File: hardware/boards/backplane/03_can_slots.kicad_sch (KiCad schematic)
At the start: 11 parts, among them J8 DC IN, U4 INA237AIDGSR

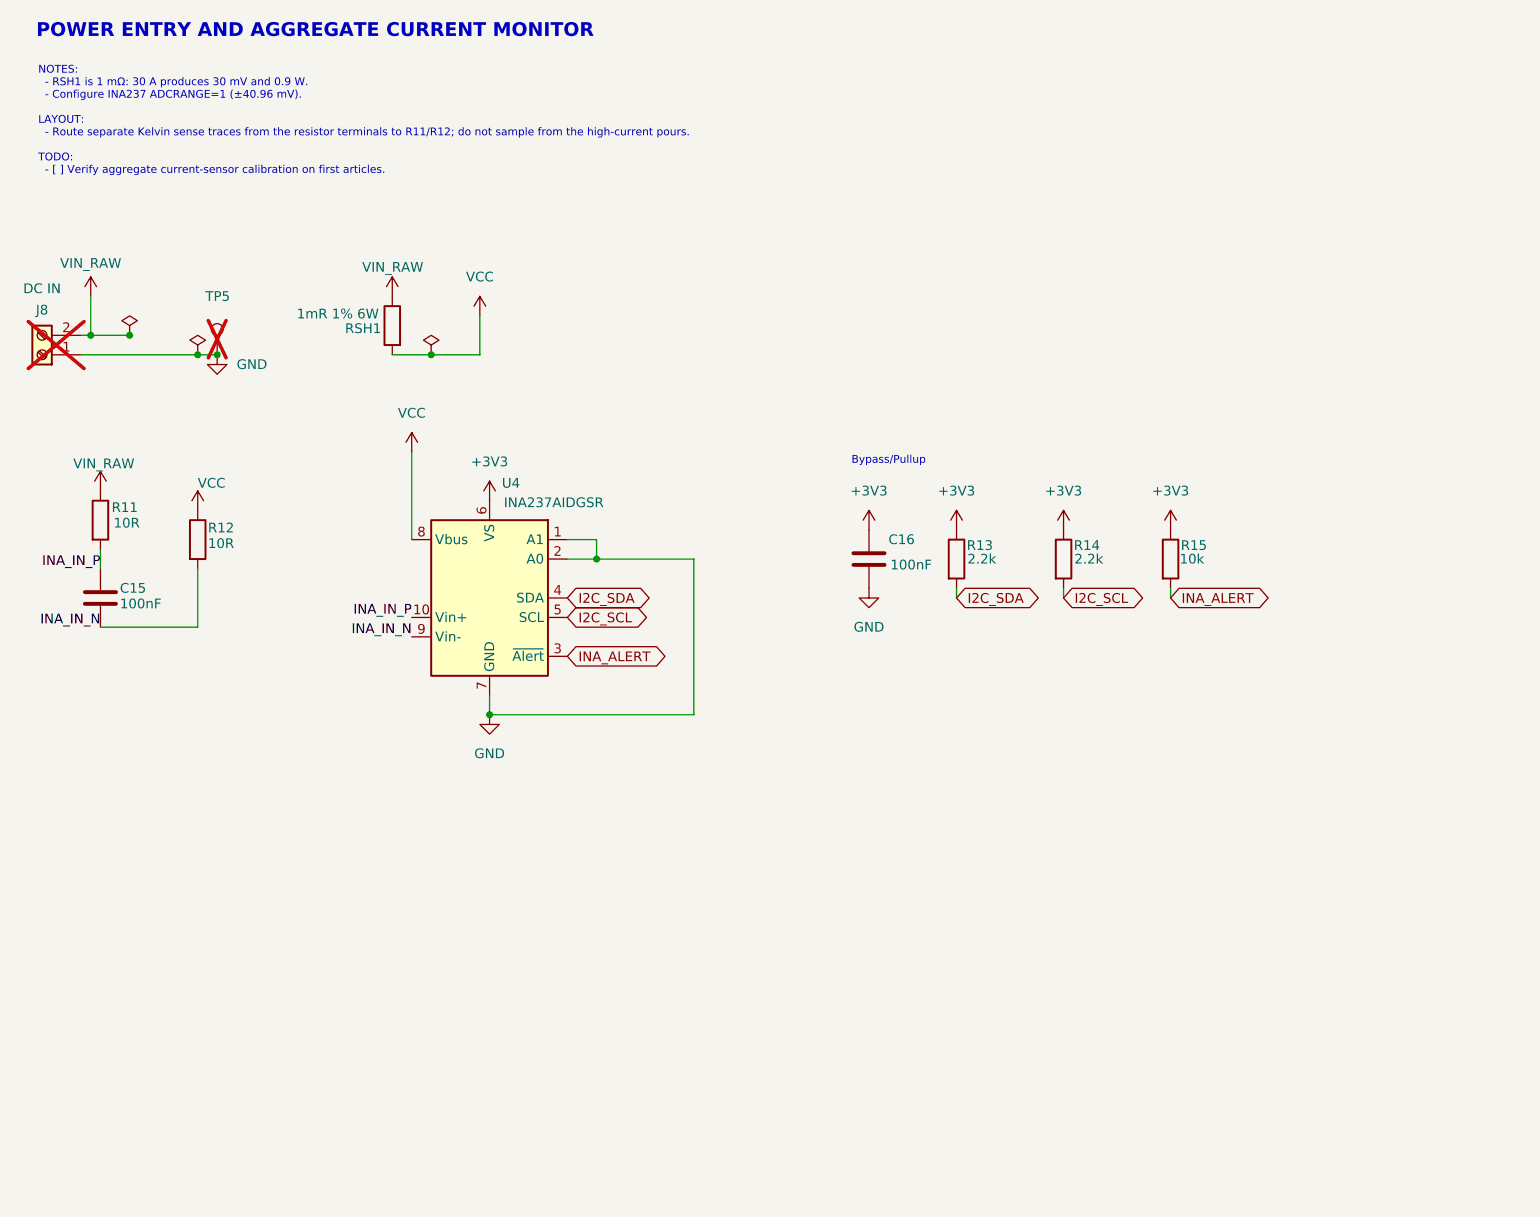
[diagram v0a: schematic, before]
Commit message: refactor: consolidate active KiCad projects under backplane and carrier
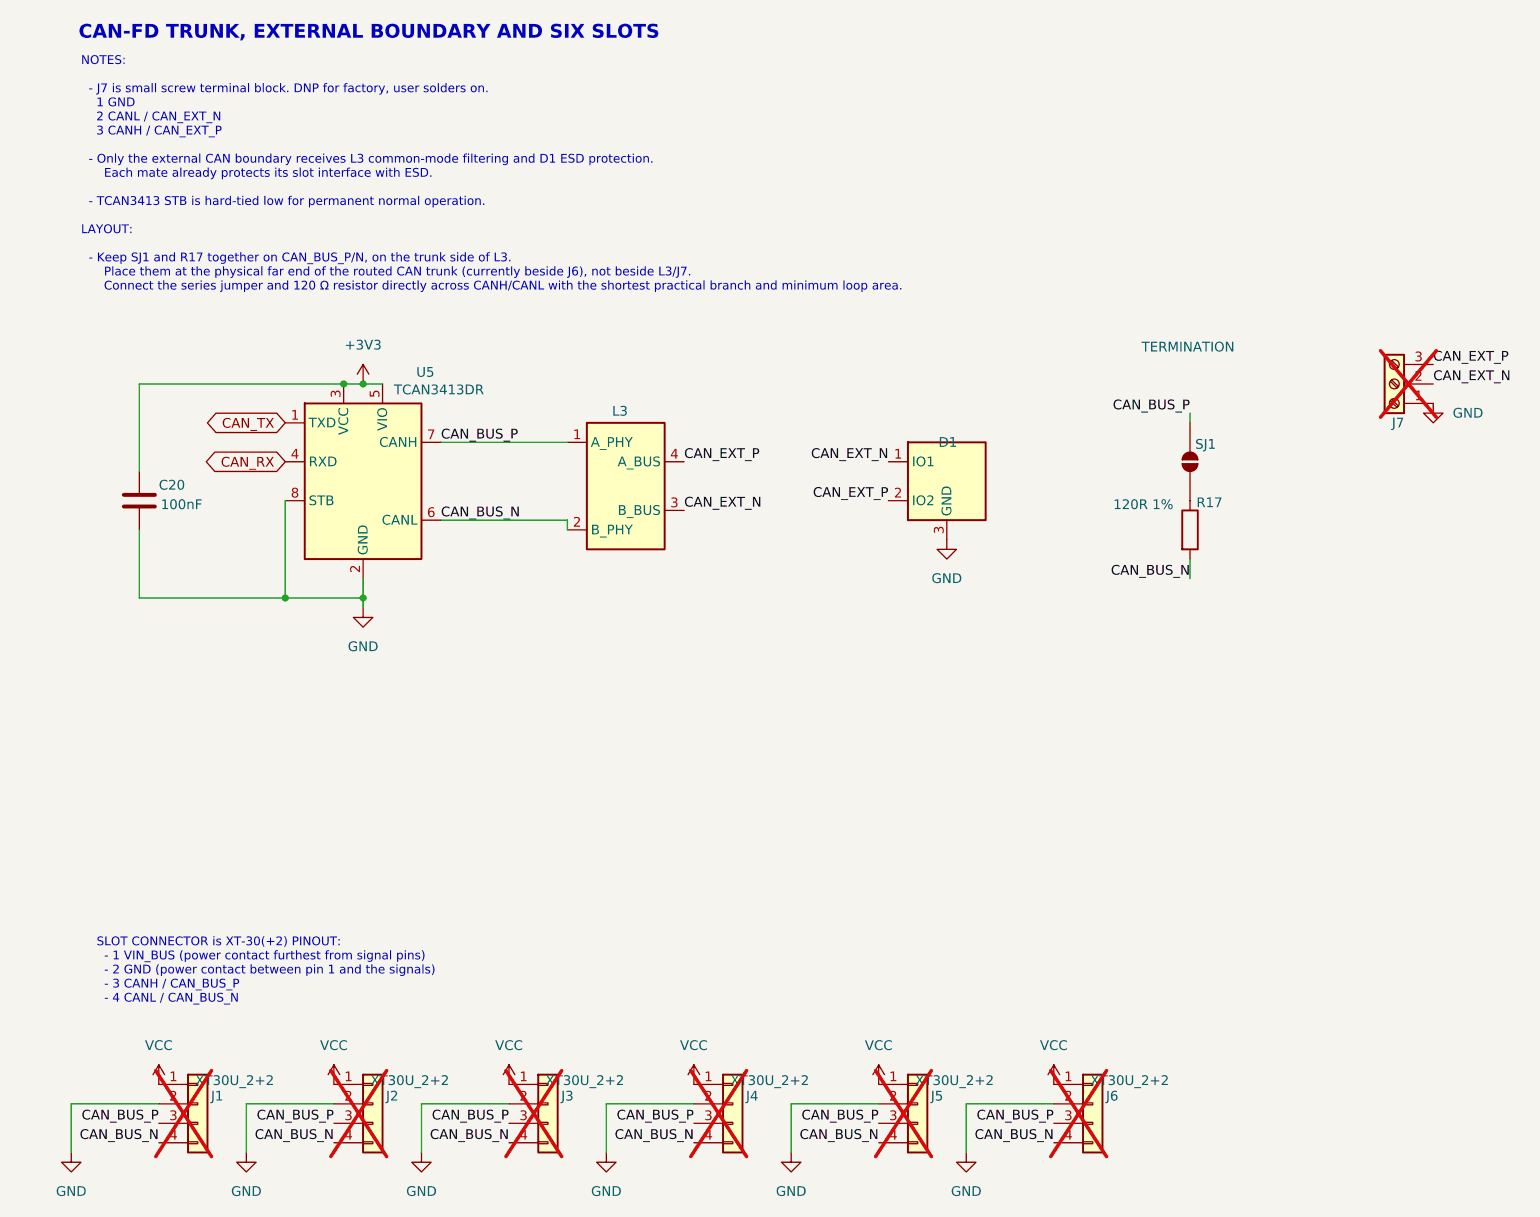
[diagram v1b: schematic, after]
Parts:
- removed C15, C16: 100nF, Capacitor_SMD:C_0603_1608Metric, symbol Device:C
- removed J8: DC IN, mini-rack-power:DORABO_DB910-6.35-2P-GN-S, symbol Connector:Screw_Terminal_01x02
- removed R11, R12: 10R, Resistor_SMD:R_0603_1608Metric, symbol Device:R
- removed R13, R14: 2.2k, Resistor_SMD:R_0603_1608Metric, symbol Device:R
- removed R15: 10k, Resistor_SMD:R_0603_1608Metric, symbol Device:R
- removed RSH1: 1mR 1% 6W, Resistor_SMD:R_2512_6332Metric, symbol Device:R
- removed TP5: GND, TestPoint:TestPoint_Pad_D1.5mm, symbol Connector:TestPoint
- removed U4: INA237AIDGSR, mini-rack-power:MSOP-10_3x3mm_P0.5mm_0.20mm_Clearance, symbol Sensor_Energy:INA237
- added C20: 100nF, Capacitor_SMD:C_0603_1608Metric, symbol Device:C
- added D1: PESD2CANFD27V-TR, Package_TO_SOT_SMD:SOT-23, symbol backplane-backpack:PESD_Dual_SOT23
- added J1, J2, J3, J4, J5, J6: XT30U_2+2, mini-rack-power:Amass_XT30U_2plus2_F, symbol Connector_Generic:Conn_01x04
- added J7: XY308-2.54-3P / EXTERNAL CAN, mini-rack-power:TerminalBlock_Xinya_XY308-2.54-3P_1x03_P2.54mm_Horizontal, symbol Connector:Screw_Terminal_01x03
- added L3: ACT1210D-101-2P-TL00, mini-rack-power:L_CommonModeChoke_TDK_ACT1210D, symbol backplane-backpack:ACT1210D_1243
- added R17: 120R 1%, Resistor_SMD:R_0603_1608Metric, symbol Device:R
- added SJ1: TERMINATION, Jumper:SolderJumper-2_P1.3mm_Open_Pad1.0x1.5mm, symbol Jumper:SolderJumper_2_Open
- added U5: TCAN3413DR, Package_SO:SOIC-8_3.9x4.9mm_P1.27mm, symbol backplane-backpack:TCAN3413DR
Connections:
- net +3V3: now also C20.1, U5.3 (VCC), U5.5 (VIO)
- net GND: now also C20.2, D1.3 (GND), J1.2 (Pin_2), J2.2 (Pin_2), J3.2 (Pin_2), J4.2 (Pin_2), J5.2 (Pin_2), J6.2 (Pin_2), J7.1 (Pin_1), U5.2 (GND), U5.8 (STB)
- net VCC: now also J1.1 (Pin_1), J2.1 (Pin_1), J3.1 (Pin_1), J4.1 (Pin_1), J5.1 (Pin_1), J6.1 (Pin_1)
- new net: R17.1, SJ1.2 (B)
- new net CAN_BUS_N: J1.4 (Pin_4), J2.4 (Pin_4), J3.4 (Pin_4), J4.4 (Pin_4), J5.4 (Pin_4), J6.4 (Pin_4), L3.2 (B_PHY), R17.2, U5.6 (CANL)
- new net CAN_BUS_P: J1.3 (Pin_3), J2.3 (Pin_3), J3.3 (Pin_3), J4.3 (Pin_3), J5.3 (Pin_3), J6.3 (Pin_3), L3.1 (A_PHY), SJ1.1 (A), U5.7 (CANH)
- new net CAN_EXT_N: D1.1 (IO1), J7.2 (Pin_2), L3.3 (B_BUS)
- new net CAN_EXT_P: D1.2 (IO2), J7.3 (Pin_3), L3.4 (A_BUS)
- new net CAN_RX: U5.4 (RXD)
- new net CAN_TX: U5.1 (TXD)
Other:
- note added: "CAN-FD TRUNK, EXTERNAL BOUNDARY AND SIX SLOTS"
- note added: "NOTES: - J7 is small screw terminal block. DNP for factory, user solders on. 1 GND 2 CANL / CAN_EXT_N 3 CANH / CAN_EXT_P - Only the external CAN boundary receives L3 common-mode filtering and D1 ESD protection. Each mate already protects its slot interface with ESD. - TCAN3413 STB is hard-tied low for permanent normal operation. LAYOUT: - Keep SJ1 and R17 together on CAN_BUS_P/N, on the trunk sid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"
- note added: "SLOT CONNECTOR is XT-30(+2) PINOUT: - 1 VIN_BUS (power contact furthest from signal pins) - 2 GND (power contact between pin 1 and the signals) - 3 CANH / CAN_BUS_P - 4 CANL / CAN_BUS_N"
- note removed: "Bypass/Pullup"
- note removed: "NOTES: - RSH1 is 1 mΩ: 30 A produces 30 mV and 0.9 W. - Configure INA237 ADCRANGE=1 (±40.96 mV). LAYOUT: - Route separate Kelvin sense traces from the resistor terminals to R11/R12; do not sample from the high-current pours. TODO:r - [ ] Verify aggregate current-sensor calibration on first articles."
- note removed: "POWER ENTRY AND AGGREGATE CURRENT MONITOR"

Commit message: Add dedicated VCC bypass capacitor for CAN transceiver
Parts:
- added C21: 100nF, Capacitor_SMD:C_0603_1608Metric, symbol Device:C
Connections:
- net +3V3: now also C21.1
- net GND: now also C21.2
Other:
- note added: "Place C21 at U5 VCC (pin 3) / GND (pin 2). Keep C20 at U5 VIO (pin 5) / GND (pin 2)."

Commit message: Give CAN VCC bypass capacitor unique C22 reference
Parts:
- renumbered C21 to C22
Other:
- note added: "Place C22 at U5 VCC (pin 3) / GND (pin 2). Keep C20 at U5 VIO (pin 5) / GND (pin 2)."
- note removed: "Place C21 at U5 VCC (pin 3) / GND (pin 2). Keep C20 at U5 VIO (pin 5) / GND (pin 2)."
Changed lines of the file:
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@@
 		)
 	)
-	(text "Place C21 at U5 VCC (pin 3) / GND (pin 2).\nKeep C20 at U5 VIO (pin 5) / GND (pin 2)."
-		(at 17.78 102.87 0)
-		(effects
-			(font
-				(size 1.143 1.143)
-			)
-			(justify left bottom)
-		)
-	)
 	(label "CAN_EXT_N"
 		(at 196.85 62.23 0)
@@
 		)
 	)
+  (text "Place C22 at U5 VCC (pin 3) / GND (pin 2).\nKeep C20 at U5 VIO (pin 5) / GND (pin 2)."
+    (at 17.78 102.87 0)
+    (effects (font (size 1.143 1.143)) (justify left bottom))
+  )
 	(symbol
 		(lib_id "power:VCC")
@@
 		(on_board yes)
 		(dnp no)
-		(property "Reference" "C21"
+		(property "Reference" "C22"
 			(at 18.415 74.93 0)
 			(effects
@@
 			(project "backplane"
 				(path "/348cc909-6345-4013-9bef-98714057a65b/eb7e4e77-e42b-4b43-976a-f7a3e8147b95"
-					(reference "C21")
+					(reference "C22")
 					(unit 1)
 				)
